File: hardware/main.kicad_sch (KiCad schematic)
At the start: 434 parts, among them J1 DS1128-09-S8B8X, J10 AS0BC21-S30BM-7H, J2 DS1128-09-S8B8X, J3 DS1128-09-S8B8X, J4 98424-G52-04ALF, J5 miniPCI-E_52P_5.2, J8 USB_C_Receptacle, J9 TYPE-C-31-M-12, Q1 SSM6J501NU, Q3 FDV301N, SW1 TS-1187A-B-A-B, SW2 TS-1187A-B-A-B, U1 SSD1306-OLED-0.91, U10 W25Q256FVEIG, U12 TPD2EUSB30, U13 TPD2EUSB30, U14 TPD2EUSB30, U15 IP5328P, U2 MT7621A, U3 TPS63020, U4 TPS63020, U5 MT3420B, U6 MT3420B, U7 MT3420B, U8 MT3420B, U9 NT5CB64M16FP-DH (!), Y1 X322540MPB4SI

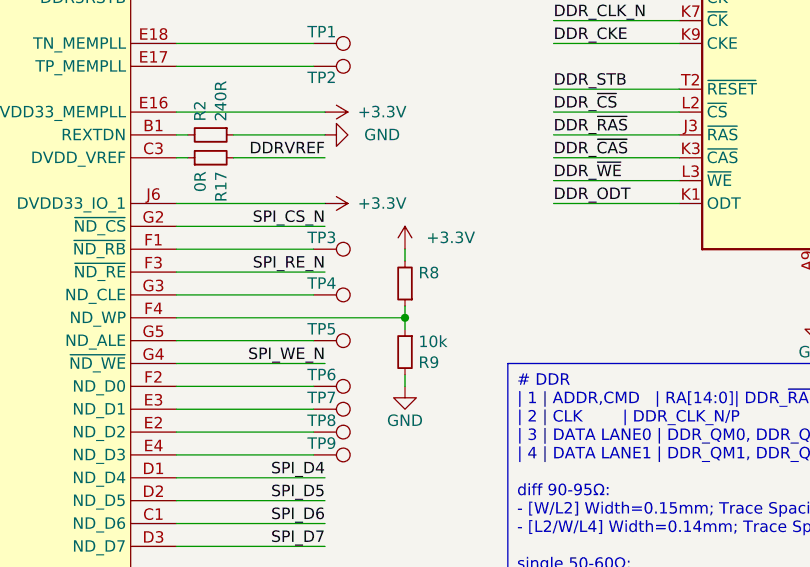
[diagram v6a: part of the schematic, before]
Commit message: fix mask via for bga
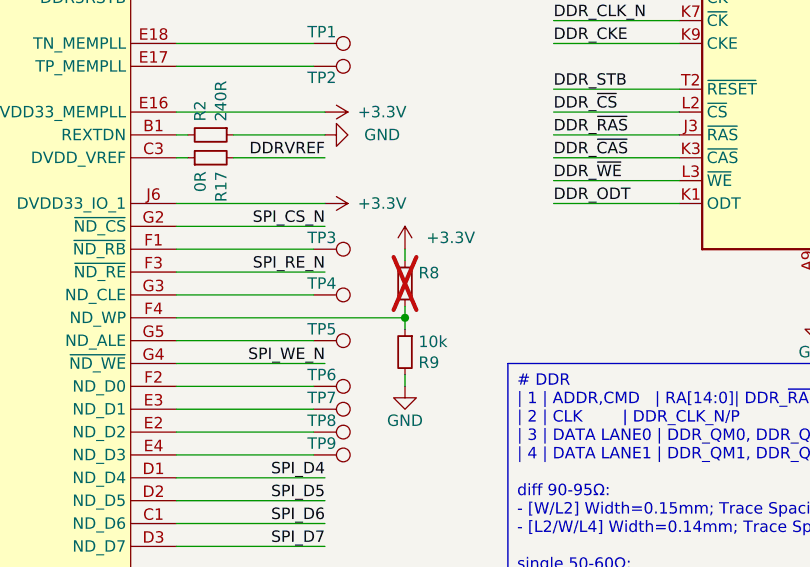
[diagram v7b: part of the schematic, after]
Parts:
- R8: now not fitted; now left out of the parts list
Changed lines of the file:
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@@
   (junction (at 708.66 135.89) (diameter 0) (color 0 0 0 0)
   )
-  (junction (at 111.76 492.76) (diameter 0) (color 0 0 0 0)
-  )
   (junction (at 775.97 69.85) (diameter 0) (color 0 0 0 0)
   )
@@
   (junction (at 407.67 58.42) (diameter 0) (color 0 0 0 0)
   )
+  (junction (at 111.76 492.76) (diameter 0) (color 0 0 0 0)
+  )
   (junction (at 713.74 135.89) (diameter 0) (color 0 0 0 0)
   )
@@
     (stroke (width 0) (type default))
   )
+  (wire (pts (xy 111.76 492.76) (xy 111.76 494.03))
+    (stroke (width 0) (type default))
+  )
   (wire (pts (xy 261.62 115.57) (xy 261.62 118.11))
     (stroke (width 0) (type default))
@@
     (stroke (width 0) (type default))
   )
-  (wire (pts (xy 111.76 492.76) (xy 111.76 494.03))
-    (stroke (width 0) (type default))
-  )
   (wire (pts (xy 410.21 200.66) (xy 410.21 201.93))
     (stroke (width 0) (type default))
@@
     (stroke (width 0) (type default))
   )
-  (wire (pts (xy 86.36 492.76) (xy 111.76 492.76))
-    (stroke (width 0) (type default))
-  )
   (wire (pts (xy 568.96 403.86) (xy 558.8 403.86))
     (stroke (width 0) (type default))
@@
     (stroke (width 0) (type default))
   )
+  (wire (pts (xy 86.36 492.76) (xy 111.76 492.76))
+    (stroke (width 0) (type default))
+  )
   (wire (pts (xy 284.48 77.47) (xy 287.02 77.47))
     (stroke (width 0) (type default))
@@
   )
   (symbol (lib_id "Device:R_Small") (at 111.76 488.95 180) (unit 1)
-    (in_bom yes) (on_board yes) (dnp no)
+    (in_bom no) (on_board yes) (dnp yes)
     (property "Reference" "R8" (at 113.2586 487.7816 0)
       (effects (font (size 1.27 1.27)) (justify right))

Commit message: add  usb hub and wifi
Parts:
- added C145, C150: 10u, Capacitor_SMD:C_0603_1608Metric, symbol Device:C_Small
- added C146, C148: 100n, Capacitor_SMD:C_0402_1005Metric, symbol Device:C_Small
- added C147, C149: 18p, Capacitor_SMD:C_0402_1005Metric, symbol Device:C_Small
- added J?: U.FL-R-SMT-1(80), MAS_Package_std:U.FL-R-SMT-1, symbol Connector_Generic:Conn_01x02
- added R164: 47k, Resistor_SMD:R_0402_1005Metric, symbol Device:R_Small
- added R165: 100k, Resistor_SMD:R_0402_1005Metric, symbol Device:R_Small
- added R167: 0R, Resistor_SMD:R_0402_1005Metric, symbol Device:R_Small
- added R168, R169, R170, R87: 4.7k, Resistor_SMD:R_0402_1005Metric, symbol Device:R_Small
- added R171: 2.7k, Resistor_SMD:R_0402_1005Metric, symbol Device:R_Small
- added TP38, TP39, TP40, TP41: TP, MAS_Package_std:TestPoint_Pad_D1mm, symbol Connector:TestPoint
- added TP42, TP43, TP44, TP45: TP, MAS_Package_std:TestPoint_Pad_D0.5mm, symbol Connector:TestPoint
- added U11: FE1.1S-BQFN24B, MAS_Package_std:WQFN-24-1EP_4x4mm_P0.5mm_EP2.45x2.45mm, symbol MAS_IC_Interface:FE1.1s
- added U16: RTL8188_module, MAS_Package_nostd:RTL8188_module, symbol MAS_Module:RTL8188_module
- added Y2: TAXM12M4RKDCDT2T, MAS_Package_std:Oscillator_SMD_SMD3225-4P, symbol Device:Crystal_GND24
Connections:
- net +3V3: now also C145.1, C148.1, C150.2, R168.1, R169.1, R87.2, U11.20 (VD33F), U16.4 (+3V3)
- net +5V: now also C146.1, R164.2
- net -BATT: now also C145.2, C146.2, C147.2, C148.2, C149.2, C150.1, J?.2 (Pin_2), R165.1, R170.2, R171.1, U11.25 (EP), U16.1 (GND), U16.5 (GND), Y2.2, Y2.4
- net PERST_N: now also R167.1
- net USB1_DN: now also U11.14 (DMU); no longer J5.36 (USB_D-)
- net USB1_DP: now also U11.15 (DPU); no longer J5.38 (USB_D+)
- new net: C149.1, U11.4 (XIN), Y2.1
- new net: C147.1, U11.3 (XOUT), Y2.3
- new net: TP44.1, U11.21 (DRV)
- new net: R170.1, U11.2 (TESTJ/EESDA)
- new net: TP39.1, U11.7 (DM3)
- new net: TP41.1, U11.5 (DM4)
- new net: R167.2, R87.1, U11.16 (~{XRSTJ})
- new net: TP43.1, U11.23 (LED2)
- new net: R169.2, U11.1 (OVCJ)
- new net: J?.1 (Pin_1), U16.6 (ANT)
- new net: R171.2, U11.13 (REXT)
- new net: R164.1, R165.2, U11.17 (VBUSM)
- new net: R168.2, U11.18 (BUSJ)
- new net: TP42.1, U11.22 (LED1)
- new net: TP45.1, U11.24 (PWRJ)
- new net: TP40.1, U11.6 (DP4)
- new net: TP38.1, U11.8 (DP3)
- new net USBh1_DN: J5.36 (USB_D-), U11.11 (DM1)
- new net USBh1_DP: J5.38 (USB_D+), U11.12 (DP1)
- new net USBh2_DN: U11.9 (DM2), U16.3 (USB_DM)
- new net USBh2_DP: U11.10 (DP2), U16.2 (USB_DP)
- no-connect marks 17 -> 33
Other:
- note added: "RTL8188"
- note added: "USB HUB"
- note removed: "SYS"
- moved on the sheet: C194, D3, R128, R129, R130, R131, R132, R133, R134, R135, R136, R137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
